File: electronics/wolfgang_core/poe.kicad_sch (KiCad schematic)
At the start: 19 parts, among them J3 RJ45 - RJE7318800140, J4 RJ45 - RJE7318800140, T1 LAN-TRANSFORMER ETH1-230L, POE, U13 LTC4263IS#PBF

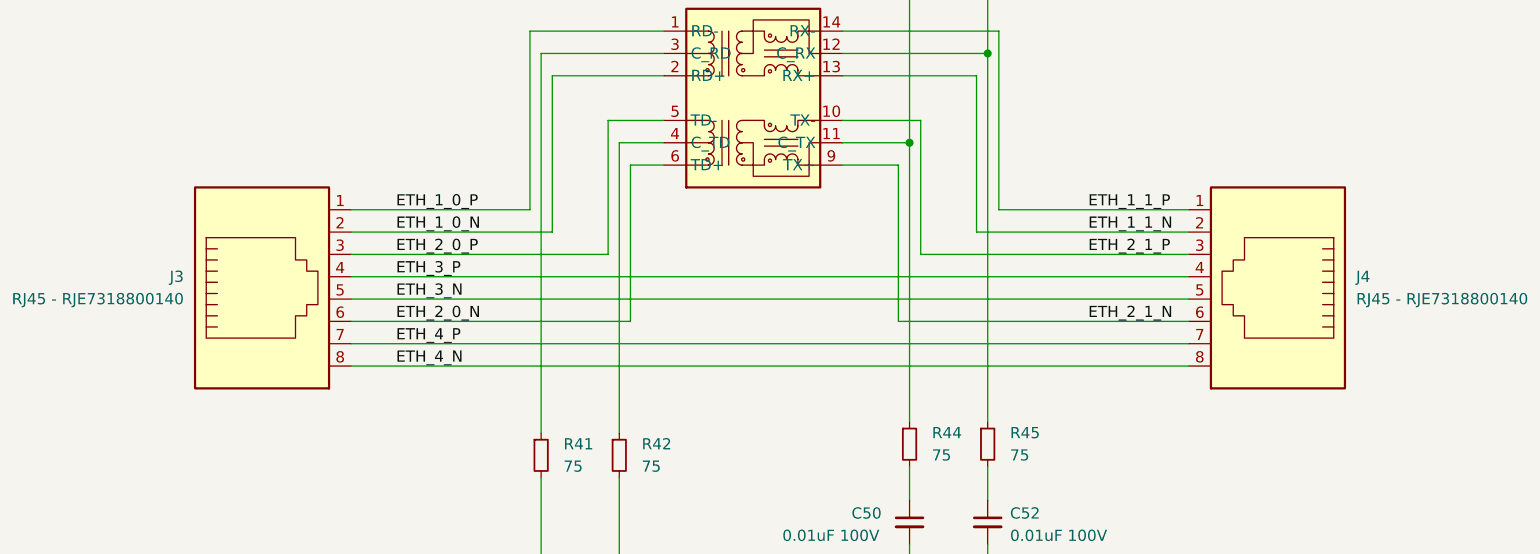
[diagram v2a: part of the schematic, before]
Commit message: Assign almost all Footprints
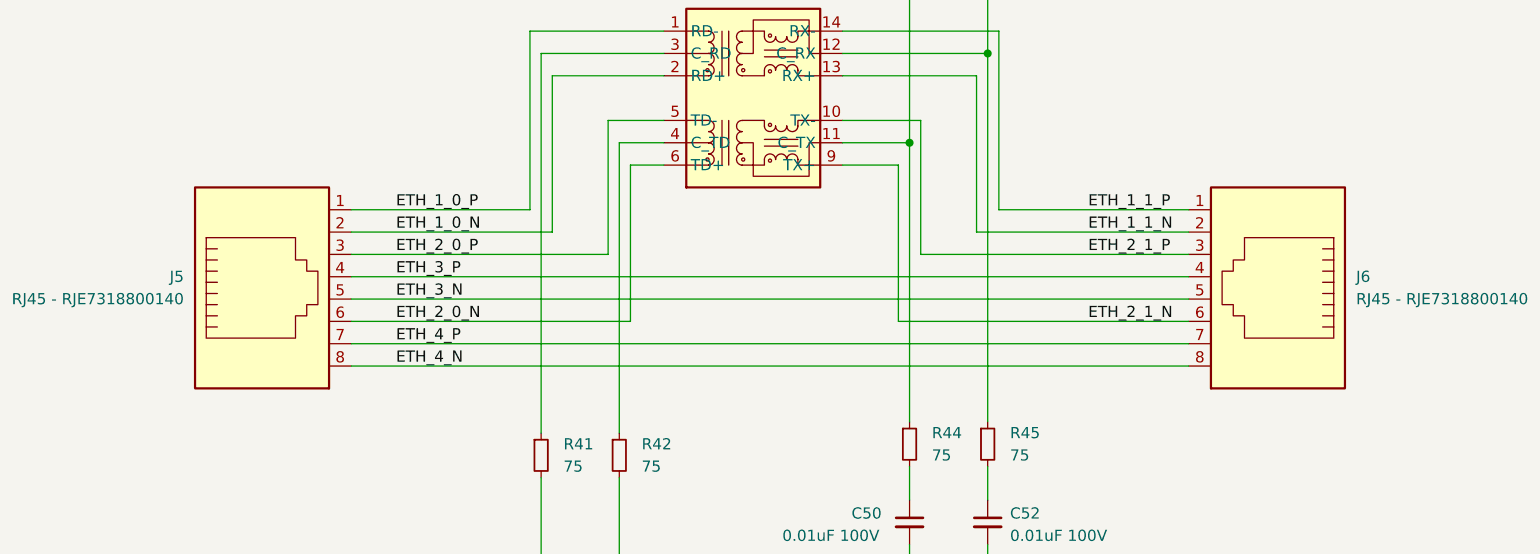
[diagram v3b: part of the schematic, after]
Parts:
- C46, C47, C48, C49, C50, C51, C52: footprint (none) -> Capacitor_SMD:C_0805_2012Metric
- D13: footprint (none) -> Diode_SMD:D_TUMD2
- D14: footprint (none) -> LED_THT:LED_D3.0mm
- F2: footprint (none) -> Fuse:Fuse_1206_3216Metric
- R41, R42, R43, R44, R45: footprint (none) -> Resistor_SMD:R_0805_2012Metric
- renumbered J3 to J5, J4 to J6
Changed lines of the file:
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@@
 			)
 		)
-		(property "Footprint" ""
+		(property "Footprint" "Resistor_SMD:R_0805_2012Metric"
 			(at 120.65 35.56 0)
 			(effects
@@
 			)
 		)
-		(property "Footprint" ""
+		(property "Footprint" "Capacitor_SMD:C_0805_2012Metric"
 			(at 153.67 160.02 0)
 			(effects
@@
 			)
 		)
-		(property "Footprint" ""
+		(property "Footprint" "Resistor_SMD:R_0805_2012Metric"
 			(at 115.57 140.97 0)
 			(effects
@@
 		(dnp no)
 		(fields_autoplaced yes)
-		(property "Reference" "#PWR0108"
+		(property "Reference" "#PWR109"
 			(at 111.76 170.18 0)
 			(effects
@@
 			(project "wolfgang_core"
 				(path "/9538e4ed-27e6-4c37-b989-9859dc0d49e8/3d827942-3ef6-4515-bd08-bedcdbccf816"
-					(reference "#PWR0108")
+					(reference "#PWR109")
 					(unit 1)
 				)
@@
 			)
 		)
-		(property "Footprint" ""
+		(property "Footprint" "Resistor_SMD:R_0805_2012Metric"
 			(at 148.59 139.7 0)
 			(effects
@@
 		(dnp no)
 		(fields_autoplaced yes)
-		(property "Reference" "#PWR0102"
+		(property "Reference" "#PWR103"
 			(at 29.21 48.26 0)
 			(effects
@@
 			(project ""
 				(path "/9538e4ed-27e6-4c37-b989-9859dc0d49e8/3d827942-3ef6-4515-bd08-bedcdbccf816"
-					(reference "#PWR0102")
+					(reference "#PWR103")
 					(unit 1)
 				)
@@
 			)
 		)
-		(property "Footprint" ""
+		(property "Footprint" "Fuse:Fuse_1206_3216Metric"
 			(at 130.81 62.738 90)
 			(effects
@@
 			)
 		)
-		(property "Footprint" ""
+		(property "Footprint" "LED_THT:LED_D3.0mm"
 			(at 120.65 25.4 0)
 			(effects
@@
 		(dnp no)
 		(fields_autoplaced yes)
-		(property "Reference" "#PWR0106"
+		(property "Reference" "#PWR107"
 			(at 86.36 58.42 0)
 			(effects
@@
 			(project ""
 				(path "/9538e4ed-27e6-4c37-b989-9859dc0d49e8/3d827942-3ef6-4515-bd08-bedcdbccf816"
-					(reference "#PWR0106")
+					(reference "#PWR107")
 					(unit 1)
 				)
@@
 		(dnp no)
 		(fields_autoplaced yes)
-		(property "Reference" "#PWR0107"
+		(property "Reference" "#PWR108"
 			(at 99.06 58.42 0)
 			(effects
@@
 			(project ""
 				(path "/9538e4ed-27e6-4c37-b989-9859dc0d49e8/3d827942-3ef6-4515-bd08-bedcdbccf816"
-					(reference "#PWR0107")
+					(reference "#PWR108")
 					(unit 1)
 				)
@@
 			)
 		)
-		(property "Footprint" ""
+		(property "Footprint" "Capacitor_SMD:C_0805_2012Metric"
 			(at 148.59 148.59 0)
 			(effects
@@
 		(dnp no)
 		(fields_autoplaced yes)
-		(property "Reference" "#PWR0109"
+		(property "Reference" "#PWR110"
 			(at 120.65 25.4 0)
 			(effects
@@
 			(project ""
 				(path "/9538e4ed-27e6-4c37-b989-9859dc0d49e8/3d827942-3ef6-4515-bd08-bedcdbccf816"
-					(reference "#PWR0109")
+					(reference "#PWR110")
 					(unit 1)
 				)
@@
 		(dnp no)
 		(fields_autoplaced yes)
-		(property "Reference" "#PWR0103"
+		(property "Reference" "#PWR104"
 			(at 46.99 44.45 0)
 			(effects
@@
 			(project ""
 				(path "/9538e4ed-27e6-4c37-b989-9859dc0d49e8/3d827942-3ef6-4515-bd08-bedcdbccf816"
-					(reference "#PWR0103")
+					(reference "#PWR104")
 					(unit 1)
 				)
@@
 		(on_board yes)
 		(dnp no)
-		(property "Reference" "J4"
+		(property "Reference" "J6"
 			(at 199.39 120.6499 0)
 			(effects
@@
 			(project "wolfgang_core"
 				(path "/9538e4ed-27e6-4c37-b989-9859dc0d49e8/3d827942-3ef6-4515-bd08-bedcdbccf816"
-					(reference "J4")
+					(reference "J6")
 					(unit 1)
 				)
@@
 			)
 		)
-		(property "Footprint" ""
+		(property "Footprint" "Capacitor_SMD:C_0805_2012Metric"
 			(at 111.76 161.29 0)
 			(effects
@@
 		(dnp no)
 		(fields_autoplaced yes)
-		(property "Reference" "#PWR0110"
+		(property "Reference" "#PWR111"
 			(at 153.67 168.91 0)
 			(effects
@@
 			(project ""
 				(path "/9538e4ed-27e6-4c37-b989-9859dc0d49e8/3d827942-3ef6-4515-bd08-bedcdbccf816"
-					(reference "#PWR0110")
+					(reference "#PWR111")
 					(unit 1)
 				)
@@
 		(dnp no)
 		(fields_autoplaced yes)
-		(property "Reference" "#PWR0105"
+		(property "Reference" "#PWR106"
 			(at 50.8 31.75 0)
 			(effects
@@
 			(project ""
 				(path "/9538e4ed-27e6-4c37-b989-9859dc0d49e8/3d827942-3ef6-4515-bd08-bedcdbccf816"
-					(reference "#PWR0105")
+					(reference "#PWR106")
 					(unit 1)
 				)
@@
 			)
 		)
-		(property "Footprint" ""
+		(property "Footprint" "Capacitor_SMD:C_0805_2012Metric"
 			(at 46.99 35.56 0)
 			(effects
@@
 			)
 		)
-		(property "Footprint" ""
+		(property "Footprint" "Resistor_SMD:R_0805_2012Metric"
 			(at 157.48 139.7 0)
 			(effects
@@
 			)
 		)
-		(property "Footprint" ""
+		(property "Footprint" "Capacitor_SMD:C_0805_2012Metric"
 			(at 139.7 64.77 0)
 			(effects
@@
 			)
 		)
-		(property "Footprint" ""
+		(property "Footprint" "Diode_SMD:D_TUMD2"
 			(at 109.22 64.77 0)
 			(effects
@@
 			)
 		)
-		(property "Footprint" ""
+		(property "Footprint" "Resistor_SMD:R_0805_2012Metric"
 			(at 106.68 140.97 0)
 			(effects
@@
 			)
 		)
-		(property "Footprint" ""
+		(property "Footprint" "Capacitor_SMD:C_0805_2012Metric"
 			(at 22.86 50.8 0)
 			(effects
@@
 		(dnp no)
 		(fields_autoplaced yes)
-		(property "Reference" "J3"
+		(property "Reference" "J5"
 			(at 66.04 120.6499 0)
 			(effects
@@
 			(project ""
 				(path "/9538e4ed-27e6-4c37-b989-9859dc0d49e8/3d827942-3ef6-4515-bd08-bedcdbccf816"
-					(reference "J3")
+					(reference "J5")
 					(unit 1)
 				)
@@
 		(dnp no)
 		(fields_autoplaced yes)
-		(property "Reference" "#PWR0104"
+		(property "Reference" "#PWR105"
 			(at 48.26 82.55 0)
 			(effects
@@
 			(project ""
 				(path "/9538e4ed-27e6-4c37-b989-9859dc0d49e8/3d827942-3ef6-4515-bd08-bedcdbccf816"
-					(reference "#PWR0104")
+					(reference "#PWR105")
 					(unit 1)
 				)
@@
 			)
 		)
-		(property "Footprint" ""
+		(property "Footprint" "Capacitor_SMD:C_0805_2012Metric"
 			(at 157.48 148.59 0)
 			(effects
@@
 		(dnp no)
 		(fields_autoplaced yes)
-		(property "Reference" "#PWR0101"
+		(property "Reference" "#PWR102"
 			(at 22.86 63.5 0)
 			(effects
@@
 			(project ""
 				(path "/9538e4ed-27e6-4c37-b989-9859dc0d49e8/3d827942-3ef6-4515-bd08-bedcdbccf816"
-					(reference "#PWR0101")
-					(unit 1)
-				)
+					(reference "#PWR102")
+					(unit 1)
+				)
